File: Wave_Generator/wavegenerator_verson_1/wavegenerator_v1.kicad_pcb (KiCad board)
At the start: 2 copper layers, 89.1 x 58 mm, 56 parts, among them J1 01x06, J2 USB_B_Micro, J3 Conn_Coaxial, J6 1x2Pinheader, SW1 button, SW2 button, SW3 SP3T, U1 ATmega328P-AU, U3 LinReg, U4 MAX038CPP, U5 MC33063AD, U7 LM318N, Y1 16MHz

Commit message: wavegenerator changes
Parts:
- added TP5: WS_0, TestPoint:TestPoint_THTPad_2.5x2.5mm_Drill1.2mm, F.Cu at (88.2, 74.7)
- added TP6: WS_1, TestPoint:TestPoint_THTPad_2.5x2.5mm_Drill1.2mm, F.Cu at (71.6, 44.8)
- added TP7: Sync, TestPoint:TestPoint_THTPad_2.5x2.5mm_Drill1.2mm, F.Cu at (71.5, 50.1)
- added TP8: output, TestPoint:TestPoint_THTPad_2.5x2.5mm_Drill1.2mm, F.Cu at (114.7, 79.8)
- C4: renamed from C16; footprint Capacitor_THT:C_Disc_D3.0mm_W1.6mm_P2.50mm -> Capacitor_THT:C_Rect_L4.0mm_W2.5mm_P2.50mm
- C5: renamed from C17; footprint Capacitor_THT:C_Disc_D3.0mm_W1.6mm_P2.50mm -> Capacitor_THT:C_Rect_L4.0mm_W2.5mm_P2.50mm
- H1, H2, H3, H4: footprint MountingHole:MountingHole_2.1mm -> MountingHole:MountingHole_3.2mm_M3
- J1: value 01x06 -> 01x05; footprint wavegenerator_v1:01x06_pin_header -> wavegenerator_v1:01x05_pin_header
- R6: renamed from R11; value 1k -> 10k
- moved C106 2.03 mm to (55.6, 97.0)
- moved C107 1.90 mm to (60.1, 97.0)
- moved R6 1.78 mm to (105.9, 83.8)
- moved R7 1.78 mm to (110.0, 83.8)
- moved H1 1.70 mm to (131.0, 45.6)
- moved H3 1.55 mm to (49.0, 45.5)
- moved H4 1.44 mm to (49.0, 98.5)
- moved H2 1.38 mm to (131.1, 98.5)
- moved U3 0.81 mm to (53.0, 90.9)
- renumbered C13 to C1, C18 to C10, C1 to C101, C2 to C102, C14 to C103, C3 to C104, C4 to C105, C8 to C106, C11 to C107, C10 to C11, C15 to C2, C12 to C3, C5 to C6, C6 to C7, C7 to C8, R6 to R1, R8 to R101, R9 to R102, R10 to R103, R1 to R104, R5 to R2, R2 to R3, R3 to R4, R4 to R5, R12 to R7
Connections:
- net Net-(J1-Pad1) renamed /MISO
- net Net-(RV3-Pad3) renamed /output
- net Net-(SW1-Pad1) renamed /switch_n
- J1 pad 2: Net-(J1-Pad2) -> /SCK
- J1 pad 3: /SCK -> /MOSI
- J1 pad 4: /MOSI -> /reset
- J1 pad 5: Net-(J1-Pad5) -> GND
- MOD1 pad 5: /reset -> /reset_lcd
- R104 pad 2: Net-(J1-Pad5) -> /reset
- SW2 pad 1: Net-(J1-Pad5) -> /reset
- U1 pad 12: Net-(U1-Pad12) -> /sync
- U1 pad 28: /reset -> /reset_lcd
- U1 pad 29: Net-(J1-Pad5) -> /reset
- U7 pad 1: GND -> Net-(U7-Pad1)
- U7 pad 5: GND -> Net-(U7-Pad5)
- U7 pad 8: GND -> Net-(U7-Pad8)
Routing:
- net /WS_1: track 35.3 -> 70.8 mm
- net Net-(J1-Pad5): track 32.2 -> 0.00 mm
- net /reset: track 11.6 -> 34.7 mm, vias 1 -> 0
- net /sync: track 25.1 -> 41.9 mm, vias 2 -> 0
- net /WS_0: track 32.4 -> 47.5 mm
- net /reset_lcd: track 0.00 -> 11.6 mm, vias 0 -> 1
- net /SCK: track 74.8 -> 66.1 mm
- net /MOSI: track 77.7 -> 69.4 mm, vias 0 -> 2
- net +3V3: track 77.0 -> 80.9 mm
- net /output: track 39.9 -> 42.2 mm
- net Net-(J3-Pad1): track 23.2 -> 22.4 mm
- net Net-(C10-Pad1): track 19.8 -> 19.0 mm
- net +5V: track 127.9 -> 127.4 mm
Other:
- board size 89.1 x 58 mm -> 89.1 x 60 mm

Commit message: touch ups
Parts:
- added R8: 10k, Resistor_THT:R_Axial_DIN0207_L6.3mm_D2.5mm_P10.16mm_Horizontal, F.Cu at (1.08, 1.53)
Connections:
- RV3 pad 2: Net-(RV3-Pad2) -> Net-(R8-Pad2)
- U4 pad 12: Net-(U4-Pad12) -> GND
- U7 pad 3: Net-(RV3-Pad2) -> Net-(R8-Pad1)

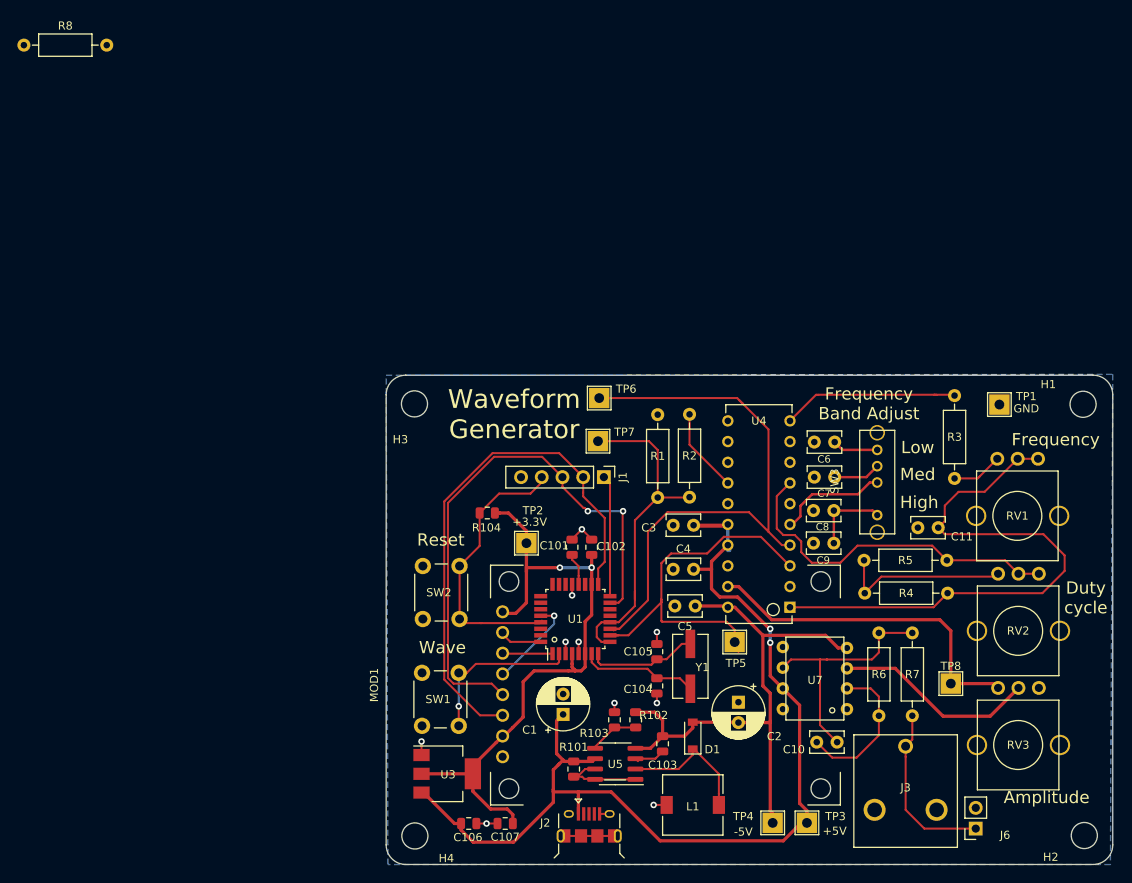
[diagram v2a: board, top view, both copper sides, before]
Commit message: removed op amp and sync connection
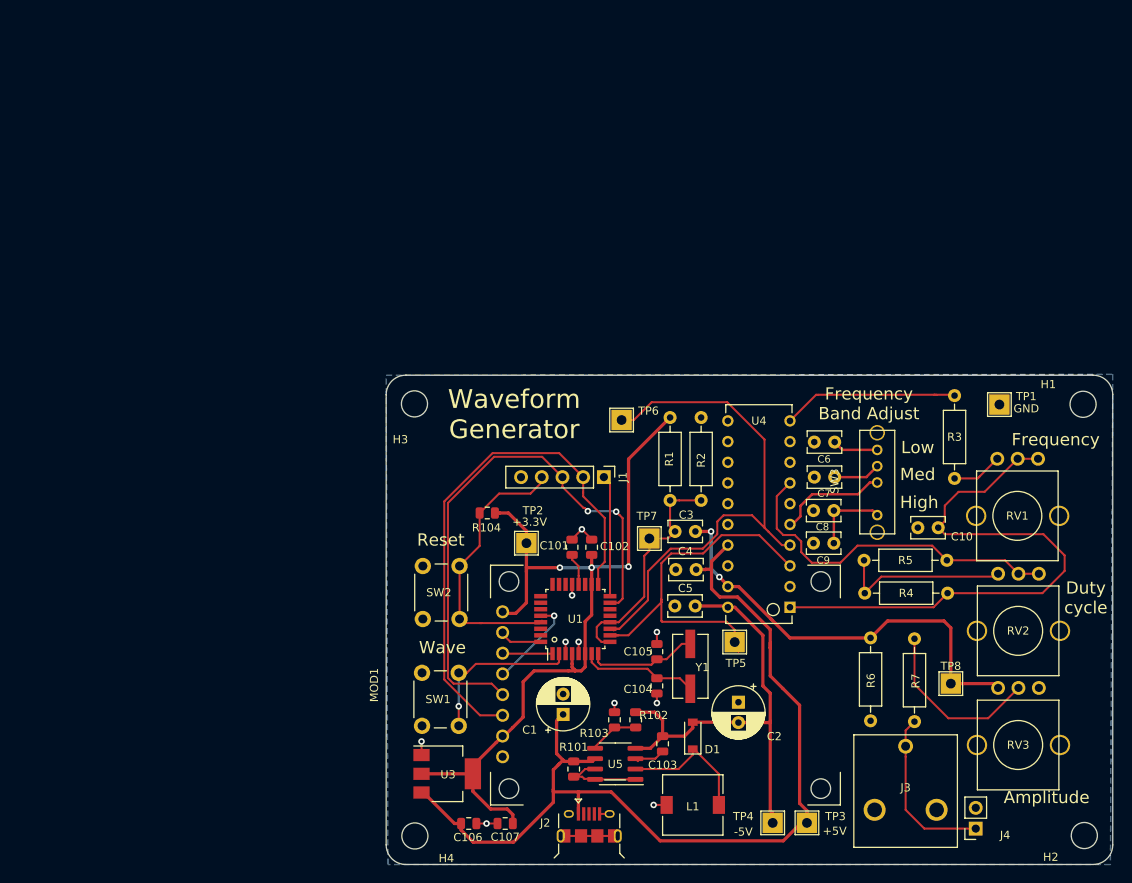
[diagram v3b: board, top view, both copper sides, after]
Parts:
- removed the C10 at (98.3, 87.0)
- removed the R7 at (110.0, 83.8)
- removed U7: LM318N, wavegenerator_v1:LM318N
- C2: value 1000uF -> 100uF
- C3: value 1uF -> 4.7uF
- R1: value 1k -> 51
- R2: value 470 -> 51
- R6: value 10k -> 100
- R7: renamed from R8; value 10k -> 560
- RV3: value 10k -> 1k
- TP7: value Sync -> freq
- moved R7 137.1 mm to (110.3, 84.5), turned to 90 degrees
- moved TP7 13.5 mm to (77.8, 62.0)
- moved R2 10.6 mm to (84.1, 57.4), turned to 90 degrees
- moved R1 9.92 mm to (80.3, 47.2), turned to 270 degrees
- moved R6 9.60 mm to (104.9, 74.2), turned to 270 degrees
- moved TP6 3.84 mm to (74.4, 47.5)
- moved C4 2.82 mm to (83.5, 65.8), turned to 180 degrees
- moved C3 2.40 mm to (80.9, 61.2), turned to 0 degrees
- renumbered C11 to C10, J6 to J4
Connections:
- C3 pad 1: +5V -> /freq
- C3 pad 2: GND -> /output
- C4 pad 1: GND -> +5V
- C4 pad 2: +5V -> GND
- R1 pad 1: /sync -> +3V3
- R1 pad 2: GND -> /freq
- R2 pad 1: Net-(R2-Pad1) -> /freq
- R2 pad 2: /sync -> GND
- R6 pad 1: Net-(C10-Pad1) (its old number) -> /output
- R6 pad 2: Net-(C10-Pad2) -> GND
- R7 pad 1: Net-(R8-Pad1) -> Net-(J3-Pad1)
- TP7 pad 1: /sync -> /freq
- U1 pad 12: /sync -> /freq
- U1 pad 9: /sync -> /freq
- U4 pad 14: Net-(R2-Pad1) -> Net-(U4-Pad14)
- U4 pad 16: +5V -> Net-(U4-Pad16)
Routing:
- net /sync: track 41.9 -> 0.00 mm
- net Net-(C10-Pad2): track 30.3 -> 0.00 mm
- net /freq: track 0.00 -> 29.3 mm
- net +3V3: track 80.9 -> 106.0 mm, vias 2 -> 3
- net Net-(RV3-Pad2): track 24.9 -> 0.00 mm
- net Net-(R7-Pad2): track 0.00 -> 21.6 mm
- net Net-(C10-Pad1) (its old number): track 19.0 -> 0.00 mm
- net /output: track 42.2 -> 53.8 mm, vias 0 -> 2
- net -5V: track 68.8 -> 57.8 mm
- net Net-(R2-Pad1): track 10.5 -> 0.00 mm
- net +5V: track 127.4 -> 117.3 mm, vias 2 -> 0
- net /WS_1: track 70.8 -> 64.2 mm
- net Net-(J3-Pad1): track 22.4 -> 21.1 mm
- net /MOSI: track 69.4 -> 68.8 mm

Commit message: numbering
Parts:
- moved J2 48.0 mm to (47.0, 56.5), turned to 270 degrees
- moved R101 1.50 mm to (67.0, 90.2)
- moved TP2 0.62 mm to (62.1, 62.6)
- renumbered U3 to U1, U1 to U2, U5 to U3
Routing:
- net +5V: track 117.3 -> 158.6 mm
- net +3V3: track 106.0 -> 104.7 mm

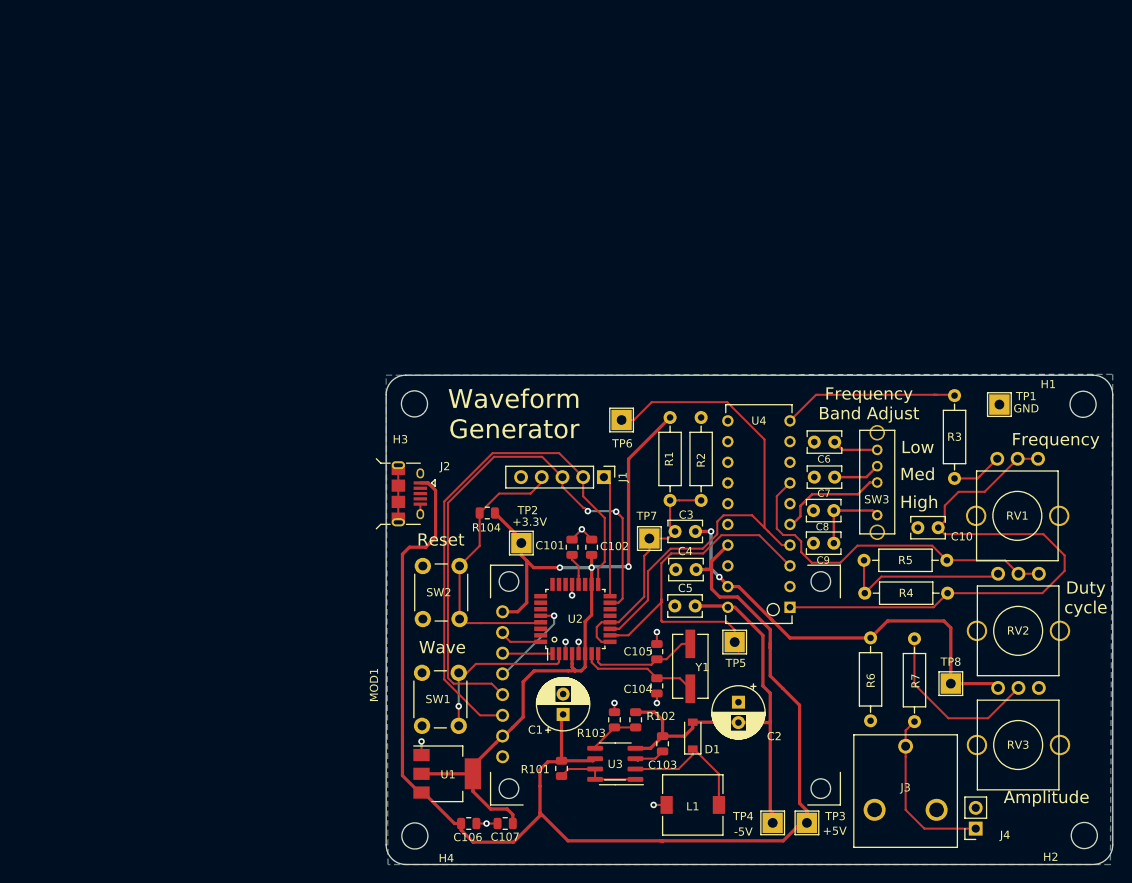
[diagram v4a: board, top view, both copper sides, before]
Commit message: adding 1nF capacitors
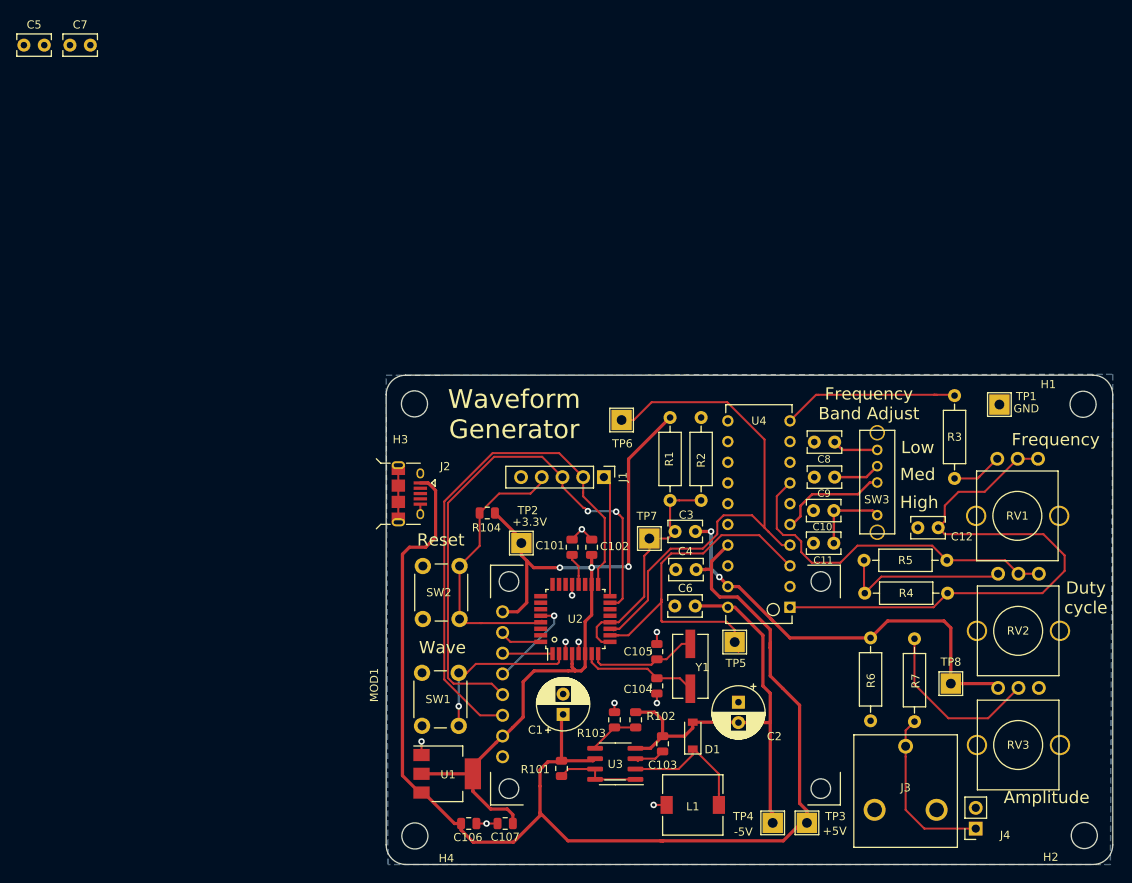
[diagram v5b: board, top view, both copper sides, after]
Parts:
- added C5: 10nF, Capacitor_THT:C_Rect_L4.0mm_W2.5mm_P2.50mm, F.Cu at (1.08, 1.53)
- added C7: 10nF, Capacitor_THT:C_Rect_L4.0mm_W2.5mm_P2.50mm, F.Cu at (6.73, 1.53)
- renumbered C8 to C10, C9 to C11, C10 to C12, C5 to C6, C6 to C8, C7 to C9

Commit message: Updated layout
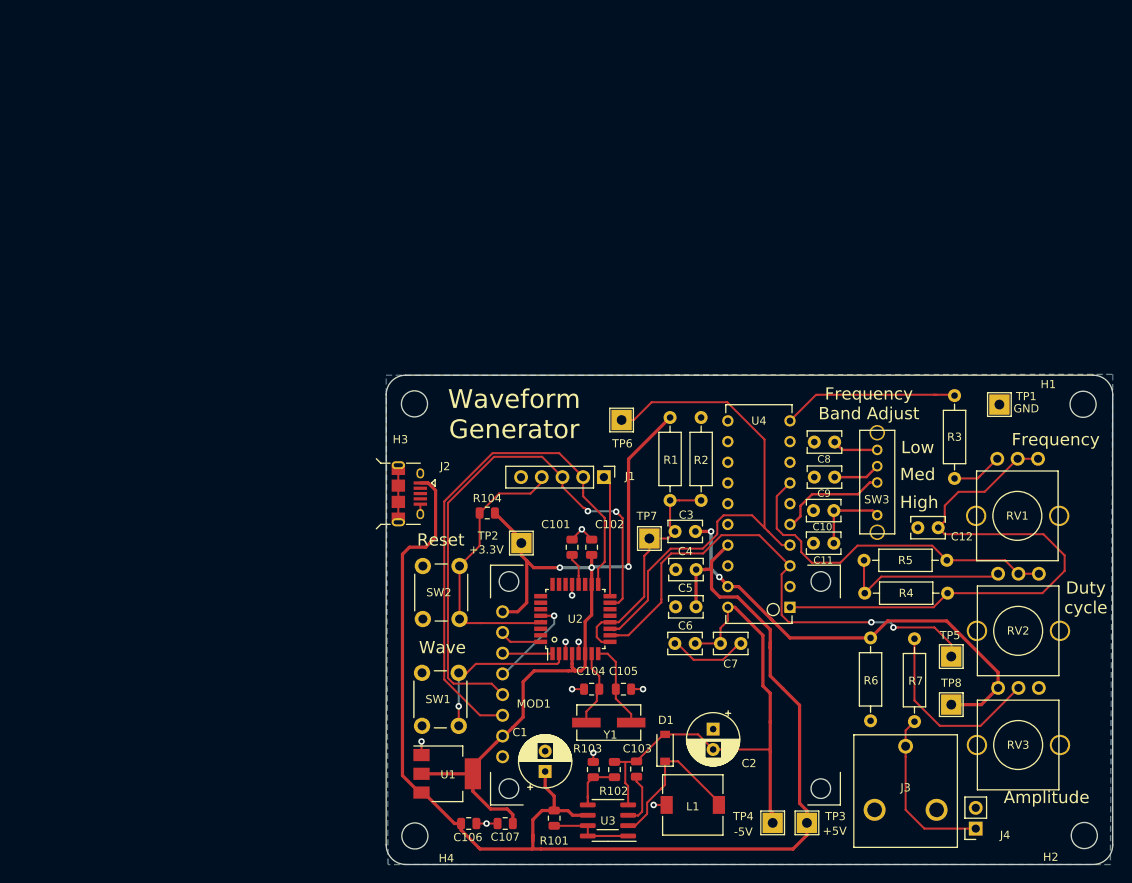
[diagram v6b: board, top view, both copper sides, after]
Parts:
- moved C7 110.2 mm to (89.0, 74.9), turned to 180 degrees
- moved C5 105.5 mm to (81.0, 70.4)
- moved TP5 26.6 mm to (114.8, 76.5), turned to 180 degrees
- moved Y1 12.1 mm to (72.8, 84.6), turned to 180 degrees
- moved C104 8.01 mm to (70.7, 80.5), turned to 0 degrees
- moved C1 7.34 mm to (65.0, 90.6)
- moved U3 7.00 mm to (72.7, 96.6)
- moved R102 6.63 mm to (73.5, 90.4)
- moved R103 6.63 mm to (70.9, 90.4)
- moved R101 6.17 mm to (66.1, 96.3)
- moved C105 6.16 mm to (74.6, 80.5), turned to 0 degrees
- moved C6 4.60 mm to (83.4, 74.9)
- moved C2 4.53 mm to (85.6, 85.4)
- moved C103 4.46 mm to (76.2, 90.3)
- moved D1 3.72 mm to (79.7, 87.7)
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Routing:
- net /WS_0: track 47.7 -> 63.0 mm, vias 0 -> 2
- net GND: track 25.5 -> 35.6 mm
- net -5V: track 57.8 -> 64.8 mm
- net Net-(C104-Pad2): track 14.5 -> 9.37 mm
- net /output: track 53.8 -> 58.3 mm
- net +5V: track 158.6 -> 161.9 mm
- net Net-(C103-Pad1): track 4.14 -> 6.88 mm
- net Net-(C105-Pad1): track 13.5 -> 10.8 mm
- net Net-(D1-Pad1): track 16.7 -> 19.3 mm
- net Net-(R7-Pad2): track 21.6 -> 23.5 mm
- net Net-(R101-Pad1): track 10.7 -> 10.0 mm

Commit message: big changes
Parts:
- added R7: 500, Resistor_THT:R_Axial_DIN0207_L6.3mm_D2.5mm_P10.16mm_Horizontal, F.Cu at (100.2, 84.4)
- R6: value 100 -> 500
- moved C7 9.38 mm to (80.8, 79.5), turned to 0 degrees
- moved R8 0.92 mm to (109.4, 84.4)
- moved TP5 0.60 mm to (114.6, 77.1)
- renumbered R7 to R8
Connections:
- R6 pad 2: GND -> Net-(R6-Pad2)
- R8 pad 2: Net-(R7-Pad2) -> Net-(R6-Pad2)
- RV3 pad 2: Net-(R7-Pad2) -> Net-(R6-Pad2)
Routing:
- net Net-(R6-Pad2): track 0.00 -> 44.3 mm
- net Net-(R7-Pad2): track 23.5 -> 0.00 mm
- net GND: track 35.6 -> 25.5 mm
- net /output: track 58.3 -> 49.8 mm
- net -5V: track 64.8 -> 67.4 mm
- net /WS_0: track 63.0 -> 63.2 mm, vias 2 -> 0

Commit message: big changes
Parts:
- removed the C11 at (100.4, 62.6)
- added R4: 1.42M, Resistor_THT:R_Axial_DIN0207_L6.3mm_D2.5mm_P10.16mm_Horizontal, F.Cu at (117.8, 54.7)
- C10: value 15pF -> 470pF
- C9: value 33nF -> 47nF
- R3: value 3.6k -> 4.87k 1%
- RV1: value 500k -> 1M
- moved TP1 48.6 mm to (72.1, 44.8)
- moved RV2 4.04 mm to (127.1, 73.9)
- moved RV1 3.96 mm to (126.9, 59.3)
- moved RV3 3.78 mm to (126.8, 87.7)
- moved TP6 2.74 mm to (72.0, 48.9)
- moved R3 0.96 mm to (114.2, 44.6)
- moved J4 0.80 mm to (118.5, 98.0), turned to 90 degrees
- renumbered C12 to C11, R8 to R10, R4 to R5, R5 to R6, R7 to R8, R6 to R9
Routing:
- net Net-(C11-Pad1): track 71.2 -> 85.5 mm
- net Net-(R10-Pad2): track 44.3 -> 52.4 mm
- net Net-(R3-Pad2): track 6.47 -> 11.2 mm
- net Net-(R5-Pad2): track 21.4 -> 26.0 mm
- net Net-(R6-Pad2): track 43.2 -> 47.4 mm
- net Net-(C10-Pad1): track 9.55 -> 5.55 mm
- net /output: track 49.8 -> 53.3 mm
- net /WS_1: track 64.2 -> 67.1 mm
- net Net-(R3-Pad1): track 21.8 -> 20.5 mm
- net Net-(J3-Pad1): track 20.8 -> 21.7 mm
